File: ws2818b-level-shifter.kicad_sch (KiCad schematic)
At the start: 7 parts, among them J101 Conn_01x03, J102 Conn_01x03, SW101 SW_SPDT, U102 74AHCT1G125

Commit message: update SPI pins for OLED
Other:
- company: (none) -> Butler Electronics
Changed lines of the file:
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@@
   (title_block
     (title "WS2812B Level Shifter")
-    (date "2023-12-24")
+    (date "2024-01-01")
     (rev "A")
+    (company "Butler Electronics")
+    (comment 1 "Joshua Butler, MD, MHI")
   )
   (junction (at 55.88 100.33) (diameter 0) (color 0 0 0 0)

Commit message: renumerate annotations
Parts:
- removed SW101: SW_SPDT, Connector_PinHeader_2.54mm:PinHeader_1x02_P2.54mm_Vertical, symbol Jumper:Jumper_2_Open
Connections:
- net LED0: now also U102.2; no longer U102.2
- net LED1: now also U102.2; no longer U102.2
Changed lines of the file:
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@@
   (junction (at 55.88 100.33) (diameter 0) (color 0 0 0 0)
-  )
-  (junction (at 82.55 45.72) (diameter 0) (color 0 0 0 0)
   )
   (junction (at 55.88 66.04) (diameter 0) (color 0 0 0 0)
@@
     (stroke (width 0) (type dash))
   )
-  (wire (pts (xy 82.55 45.72) (xy 82.55 53.34))
-    (stroke (width 0) (type default))
-  )
   (wire (pts (xy 86.36 58.42) (xy 90.17 58.42))
     (stroke (width 0) (type default))
@@
     (stroke (width 0) (type default))
   )
-  (wire (pts (xy 96.52 43.18) (xy 96.52 45.72))
-    (stroke (width 0) (type default))
-  )
   (wire (pts (xy 60.96 80.01) (xy 67.31 80.01))
     (stroke (width 0) (type default))
@@
     (stroke (width 0) (type default))
   )
-  (wire (pts (xy 82.55 53.34) (xy 90.17 53.34))
+  (wire (pts (xy 86.36 53.34) (xy 90.17 53.34))
     (stroke (width 0) (type default))
   )
   (wire (pts (xy 67.31 80.01) (xy 67.31 100.33))
-    (stroke (width 0) (type default))
-  )
-  (wire (pts (xy 85.09 45.72) (xy 82.55 45.72))
     (stroke (width 0) (type default))
   )
@@
     (stroke (width 0) (type default))
   )
-  (wire (pts (xy 82.55 43.18) (xy 82.55 45.72))
+  (wire (pts (xy 86.36 50.8) (xy 86.36 53.34))
     (stroke (width 0) (type default))
   )
   (wire (pts (xy 67.31 66.04) (xy 55.88 66.04))
-    (stroke (width 0) (type default))
-  )
-  (wire (pts (xy 96.52 45.72) (xy 95.25 45.72))
     (stroke (width 0) (type default))
   )
@@
     (effects (font (size 1.27 1.27)) (justify right bottom))
   )
-  (hierarchical_label "LED_PWR" (shape output) (at 82.55 43.18 90) (fields_autoplaced)
+  (hierarchical_label "LED_PWR" (shape output) (at 86.36 50.8 90) (fields_autoplaced)
     (effects (font (size 1.27 1.27)) (justify left))
   )
-  (hierarchical_label "LED1" (shape input) (at 45.72 90.17 180) (fields_autoplaced)
+  (hierarchical_label "LED1" (shape input) (at 45.72 55.88 180) (fields_autoplaced)
     (effects (font (size 1.27 1.27)) (justify right))
   )
@@
     (effects (font (size 1.27 1.27)) (justify left))
   )
-  (hierarchical_label "LED0" (shape input) (at 45.72 55.88 180) (fields_autoplaced)
+  (hierarchical_label "LED0" (shape input) (at 45.72 90.17 180) (fields_autoplaced)
     (effects (font (size 1.27 1.27)) (justify right))
   )
@@
       (project "stm32-snake-controller"
         (path "/dca7e15e-20a1-43f3-a9cb-86a6d7aa4e87/14bc5d8e-fdf7-4a51-a138-24c07a8ed6f6"
-          (reference "#PWR0306") (unit 1)
+          (reference "#PWR0305") (unit 1)
         )
       )
@@
     )
   )
-  (symbol (lib_id "power:VBUS") (at 96.52 43.18 0) (unit 1)
-    (in_bom yes) (on_board yes) (dnp no) (fields_autoplaced)
-    (property "Reference" "#PWR0307" (at 96.52 46.99 0)
-      (effects (font (size 1.27 1.27)) hide)
-    )
-    (property "Value" "VBUS" (at 96.52 38.1 0)
-      (effects (font (size 1.27 1.27)))
-    )
-    (property "Footprint" "" (at 96.52 43.18 0)
-      (effects (font (size 1.27 1.27)) hide)
-    )
-    (property "Datasheet" "" (at 96.52 43.18 0)
-      (effects (font (size 1.27 1.27)) hide)
-    )
-    (pin "1")
-    (instances
-      (project "stm32-snake-controller"
-        (path "/dca7e15e-20a1-43f3-a9cb-86a6d7aa4e87/14bc5d8e-fdf7-4a51-a138-24c07a8ed6f6"
-          (reference "#PWR0307") (unit 1)
-        )
-      )
-    )
-  )
   (symbol (lib_id "Connector_Generic:Conn_01x03") (at 95.25 90.17 0) (mirror x) (unit 1)
     (in_bom no) (on_board yes) (dnp no)
@@
       (project "stm32-snake-controller"
         (path "/dca7e15e-20a1-43f3-a9cb-86a6d7aa4e87/14bc5d8e-fdf7-4a51-a138-24c07a8ed6f6"
-          (reference "#PWR0303") (unit 1)
+          (reference "#PWR0304") (unit 1)
         )
       )
@@
       (project "stm32-snake-controller"
         (path "/dca7e15e-20a1-43f3-a9cb-86a6d7aa4e87/14bc5d8e-fdf7-4a51-a138-24c07a8ed6f6"
-          (reference "#PWR0304") (unit 1)
-        )
-      )
-    )
-  )
-  (symbol (lib_id "Jumper:Jumper_2_Open") (at 90.17 45.72 0) (unit 1)
-    (in_bom no) (on_board yes) (dnp no) (fields_autoplaced)
-    (property "Reference" "SW101" (at 90.17 41.91 0)
-      (effects (font (size 1.27 1.27)))
-    )
-    (property "Value" "SW_SPDT" (at 90.17 40.64 0)
-      (effects (font (size 1.27 1.27)) hide)
-    )
-    (property "Footprint" "Connector_PinHeader_2.54mm:PinHeader_1x02_P2.54mm_Vertical" (at 90.17 45.72 0)
-      (effects (font (size 1.27 1.27)) hide)
-    )
-    (property "Datasheet" "~" (at 90.17 45.72 0)
-      (effects (font (size 1.27 1.27)) hide)
-    )
-    (property "LCSC" "" (at 90.17 45.72 0)
-      (effects (font (size 1.27 1.27)) hide)
-    )
-    (pin "1")
-    (pin "2")
-    (instances
-      (project "wled-esp32-control-board"
-        (path "/39949f26-7b4e-4f4c-975a-4ef261468b2a"
-          (reference "SW101") (unit 1)
-        )
-      )
-      (project "stm32-snake-controller"
-        (path "/dca7e15e-20a1-43f3-a9cb-86a6d7aa4e87/14bc5d8e-fdf7-4a51-a138-24c07a8ed6f6"
-          (reference "SW301") (unit 1)
+          (reference "#PWR0306") (unit 1)
         )
       )
@@
       (project "stm32-snake-controller"
         (path "/dca7e15e-20a1-43f3-a9cb-86a6d7aa4e87/14bc5d8e-fdf7-4a51-a138-24c07a8ed6f6"
-          (reference "#PWR0305") (unit 1)
+          (reference "#PWR0302") (unit 1)
         )
       )
@@
       (project "stm32-snake-controller"
         (path "/dca7e15e-20a1-43f3-a9cb-86a6d7aa4e87/14bc5d8e-fdf7-4a51-a138-24c07a8ed6f6"
-          (reference "#PWR0302") (unit 1)
-        )
-      )
+          (reference "#PWR0303") (unit 1)
+        )
+      )

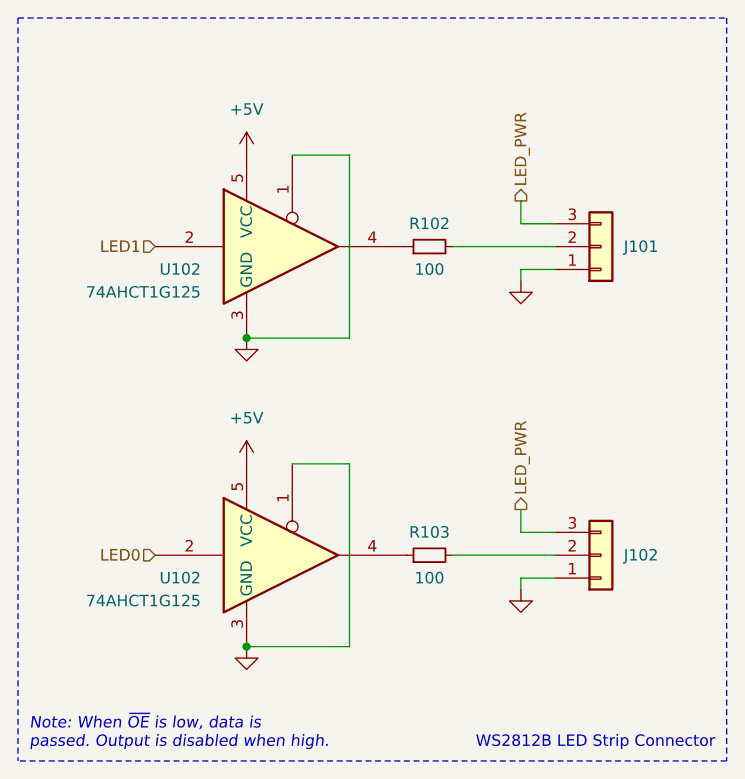
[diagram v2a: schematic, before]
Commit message: update schematic and pcb design to rev-b
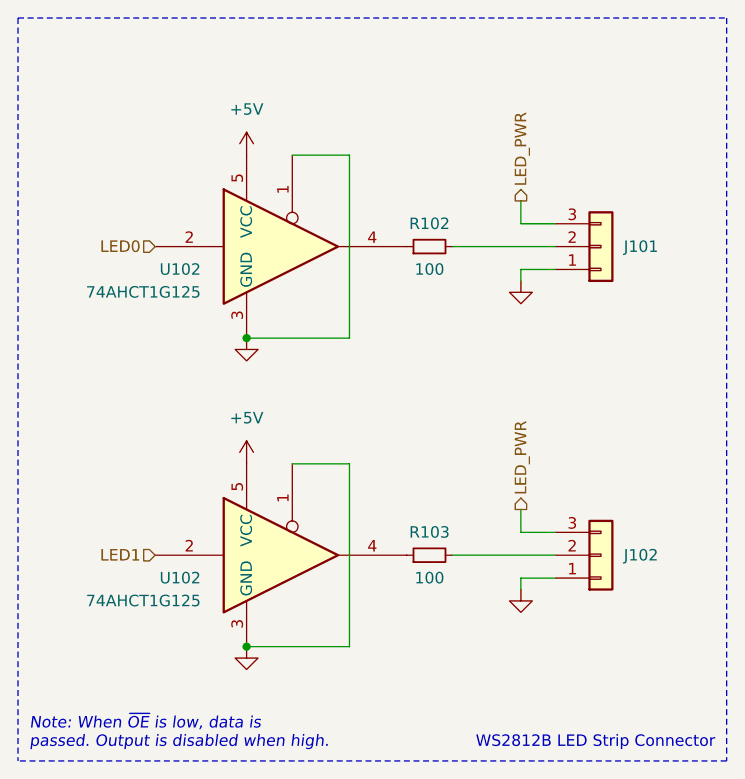
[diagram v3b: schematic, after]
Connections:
- net LED0: now also U102.2; no longer U102.2
- net LED1: now also U102.2; no longer U102.2
